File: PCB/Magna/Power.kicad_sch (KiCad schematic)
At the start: 33 parts, among them U901 AMS1117-5.0, U902 WS3222D, U903 TPS61040DBV, U904 XL1509-ADJ

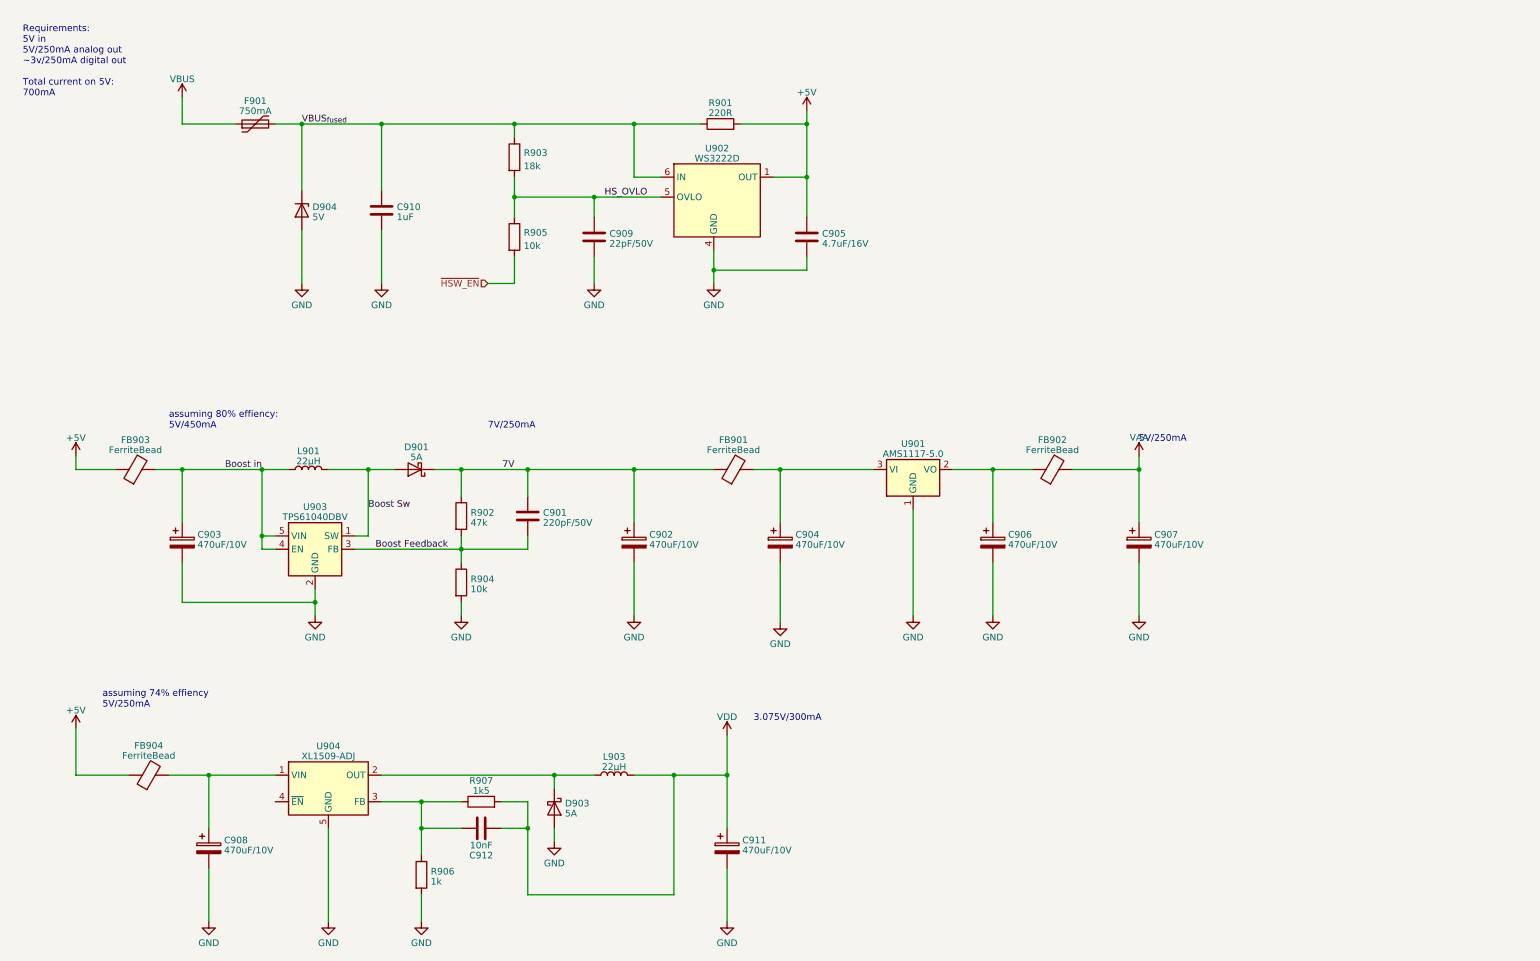
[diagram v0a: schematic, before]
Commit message: Update analogue frontend and add potentiometer interface
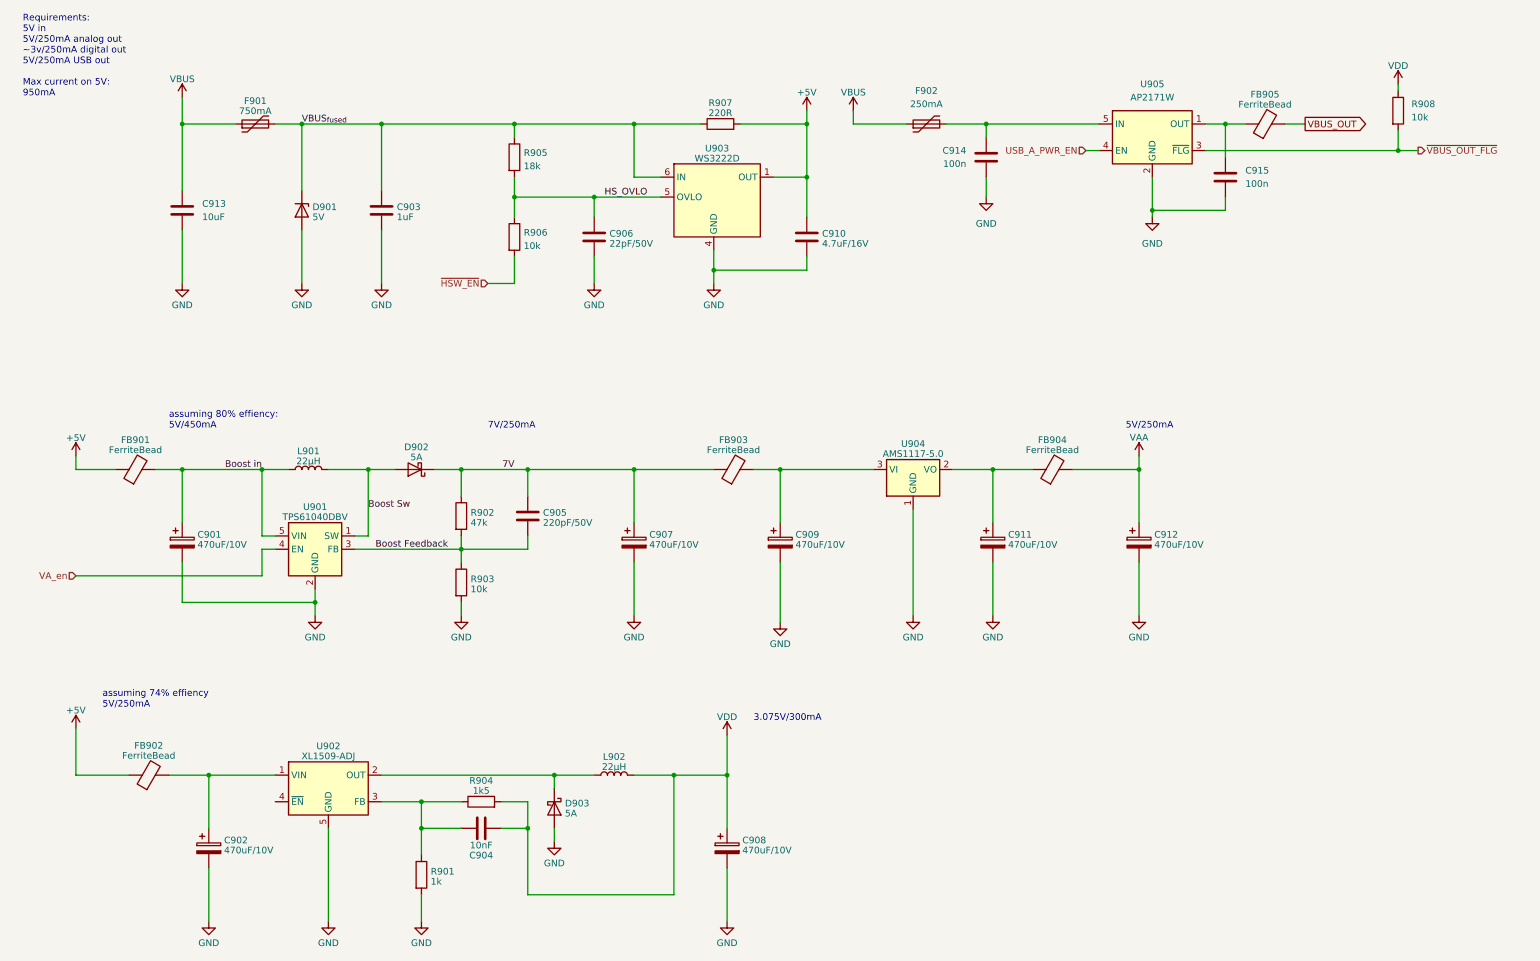
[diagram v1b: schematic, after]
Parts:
- added C913: 10uF, symbol Device:C
- added C914, C915: 100n, symbol Device:C
- added F902: 250mA, symbol Device:Polyfuse
- added FB905: FerriteBead, Inductor_SMD:L_0805_2012Metric, symbol Device:FerriteBead
- added R908: 10k, symbol Device:R
- added U905: AP2171W, Package_TO_SOT_SMD:SOT-23-5, symbol Power_Management:AP2171W
- renumbered C903 to C901, C908 to C902, C910 to C903, C912 to C904, C901 to C905, C909 to C906, C902 to C907, C911 to C908, C904 to C909, C905 to C910, C906 to C911, C907 to C912, D904 to D901, D901 to D902, FB903 to FB901, FB904 to FB902, FB901 to FB903, FB902 to FB904, L903 to L902, R906 to R901, R904 to R903, R907 to R904, R903 to R905, R905 to R906, R901 to R907, U903 to U901, U904 to U902, U902 to U903, U901 to U904
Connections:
- net Boost in: no longer U901.4 (EN)
- net GND: now also C913.2, C914.2, C915.2, U905.2 (GND)
- net VBUS: now also C913.1, F902.1
- net VDD: now also R908.1
- new net: C915.1, FB905.1, U905.1 (OUT)
- new net: C914.1, F902.2, U905.5 (IN)
- new net USB_A_PWR_EN: U905.4 (EN)
- new net VA_en: U901.4 (EN)
- new net VBUS_OUT: FB905.2
- new net ~{VBUS_OUT_FLG}: R908.2, U905.3 (~{FLG})
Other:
- note added: "Requirements: 5V in 5V/250mA analog out ~3v/250mA digital out 5V/250mA USB out Max current on 5V: 950mA"
- note removed: "Requirements: 5V in 5V/250mA analog out ~3v/250mA digital out Total current on 5V: 700mA"

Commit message: Add final touched to all schematics
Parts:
- renumbered C913 to C901, C901 to C902, C902 to C903, C903 to C904, C904 to C905, C905 to C906, C906 to C907, C907 to C908, C908 to C909, C909 to C910, C910 to C911, C914 to C912, C911 to C913, C912 to C914
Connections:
- no-connect marks 0 -> 1
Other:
- added sheet Power LED (power_led.kicad_sch)
- note added: "Requirements: 5V in 5V/250mA analog out ~3v/250mA digital out 5V/250mA USB out Max current on 5V: 950mA + eventual USB sink"
- note removed: "Requirements: 5V in 5V/250mA analog out ~3v/250mA digital out 5V/250mA USB out Max current on 5V: 950mA"
- moved on the sheet: FB905

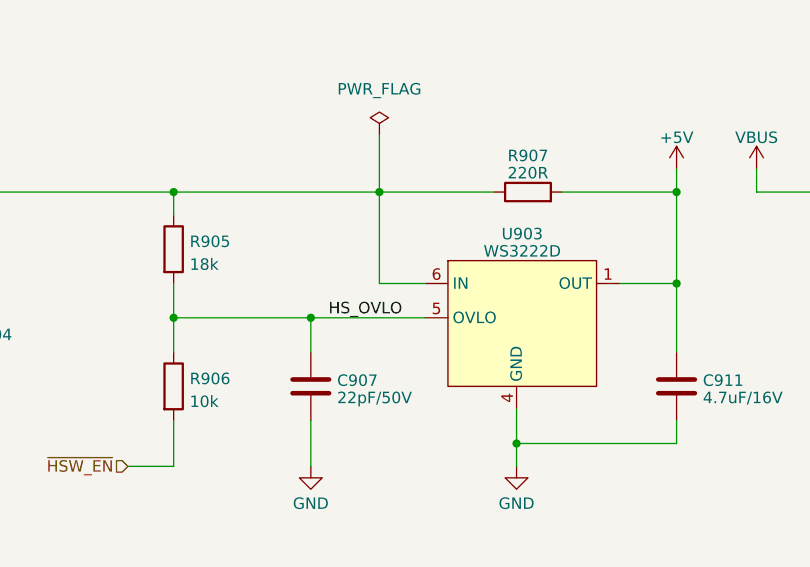
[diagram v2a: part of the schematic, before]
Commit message: Remove all ERC in schematics
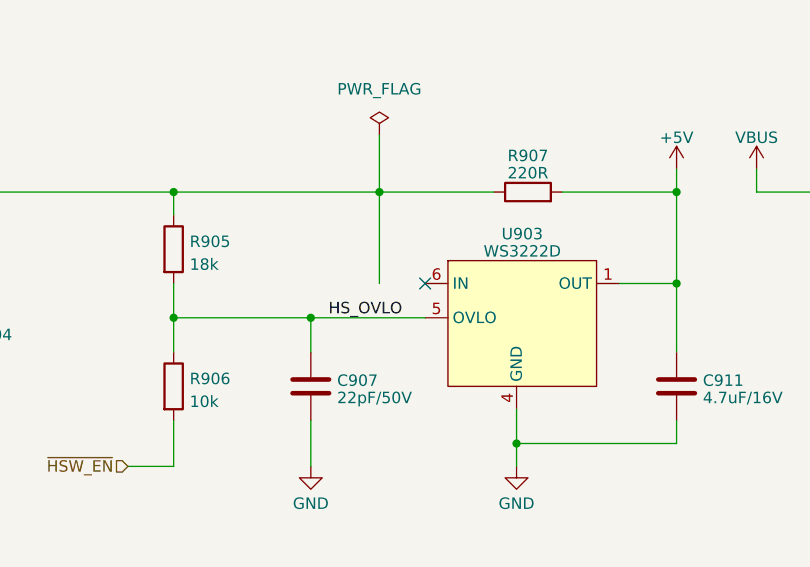
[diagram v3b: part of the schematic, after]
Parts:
- U903: symbol Skrooterlib:WS3222D -> Skrooter_symbols:WS3222D
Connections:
- net IN: no longer C904.1, D901.1 (K), F901.2, R905.1, R907.1
- new net VBUS_{fused}: C904.1, D901.1 (K), F901.2, R905.1, R907.1
- no-connect marks 1 -> 2
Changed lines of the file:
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@@
   )
   (no_connect (at 63.5 165.1))
+  (no_connect (at 137.16 45.72))
   (wire (pts (xy 106.68 170.18) (xy 111.76 170.18))
     (stroke (width 0) (type default))
@@
   )
   (wire (pts (xy 78.74 114.3) (xy 81.28 114.3))
-    (stroke (width 0) (type default))
-  )
-  (wire (pts (xy 137.16 45.72) (xy 132.08 45.72))
     (stroke (width 0) (type default))
   )
@@
     )
   )
-  (symbol (lib_id "Skrooterlib:WS3222D") (at 147.32 43.18 0) (unit 1)
+  (symbol (lib_id "Skrooter_symbols:WS3222D") (at 147.32 43.18 0) (unit 1)
     (in_bom yes) (on_board yes) (dnp no) (fields_autoplaced)
     (property "Reference" "U903" (at 147.955 40.2209 0)

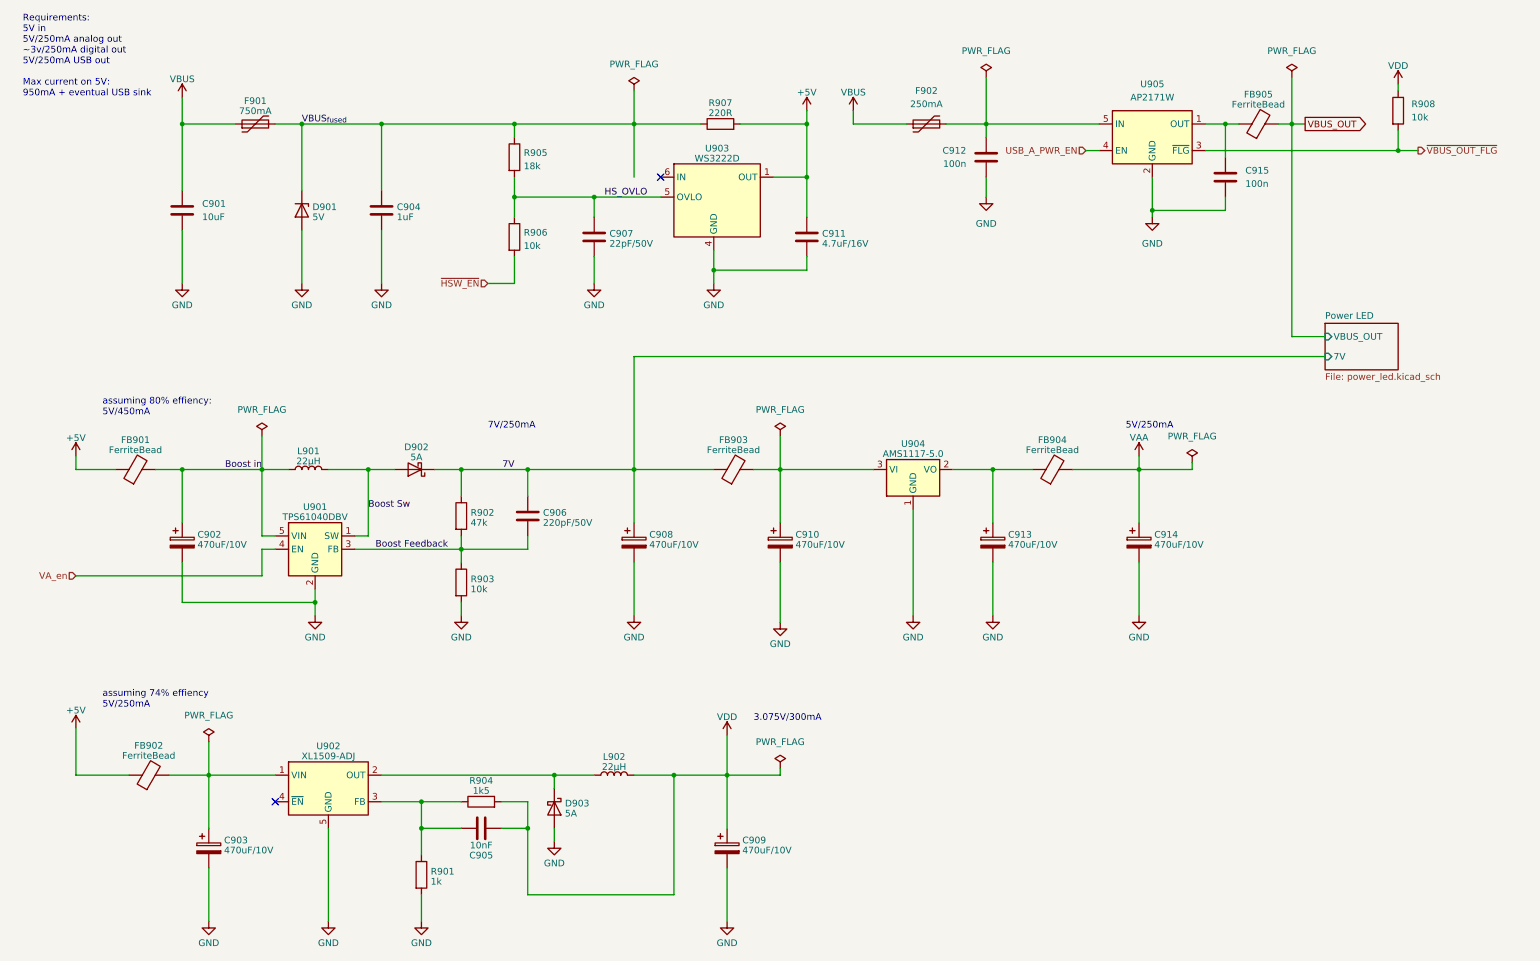
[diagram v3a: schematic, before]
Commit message: Update capacitors to parts in JLC library
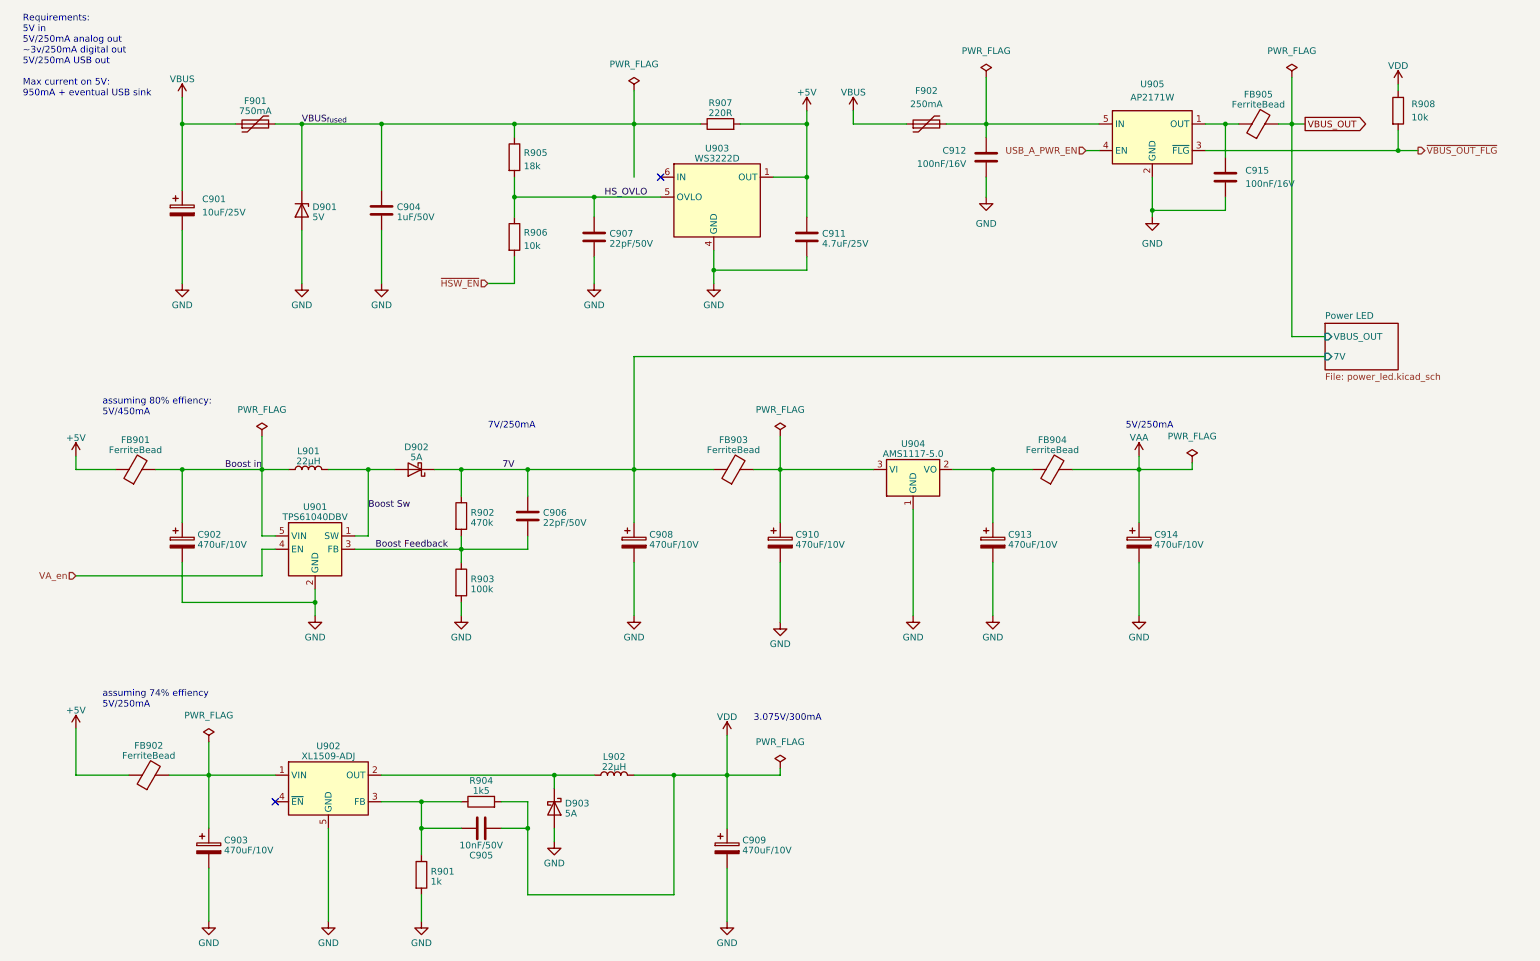
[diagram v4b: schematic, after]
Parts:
- removed C901: 10uF, symbol Device:C
- added C901: 10uF/25V, Capacitor_SMD:CP_Elec_4x5.8, symbol Device:C_Polarized
- C902, C903, C908, C909, C910, C913, C914: LCSC C2858856 -> C2163263
- C904: value 1uF -> 1uF/50V; footprint Capacitor_SMD:C_0603_1608Metric -> Capacitor_SMD:C_0805_2012Metric; LCSC C15849 -> C28323
- C905: value 10nF -> 10nF/50V; footprint Resistor_SMD:R_0402_1005Metric -> Capacitor_SMD:C_0805_2012Metric; LCSC (none) -> C3908881
- C906: value 220pF/50V -> 22pF/50V; footprint Capacitor_SMD:C_0402_1005Metric -> Capacitor_SMD:C_0805_2012Metric; LCSC C1530 -> C1804
- C907: footprint (none) -> Capacitor_SMD:C_0805_2012Metric; LCSC C1555 -> C1804
- C911: value 4.7uF/16V -> 4.7uF/25V; footprint Capacitor_SMD:C_0603_1608Metric -> Capacitor_SMD:C_0805_2012Metric; LCSC C19666 -> C1779
- C912, C915: value 100n -> 100nF/16V; footprint (none) -> Capacitor_SMD:C_0805_2012Metric; LCSC (none) -> C218638
- D901: LCSC C2925443 -> (none)
- D902, D903: LCSC C22452 -> (none)
- R901: LCSC C11702 -> (none)
- R902: value 47k -> 470k; LCSC C25792 -> (none)
- R903: value 10k -> 100k; LCSC C25744 -> (none)
- R904: LCSC C25867 -> (none)
- R905: LCSC C25762 -> (none)
- R906: LCSC C25744 -> (none)
- R907: LCSC C17557 -> (none)
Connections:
- net GND: now also C901.2
- net VBUS: now also C901.1
